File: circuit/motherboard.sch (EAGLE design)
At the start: 8 parts, among them IC1 ATMEGA8

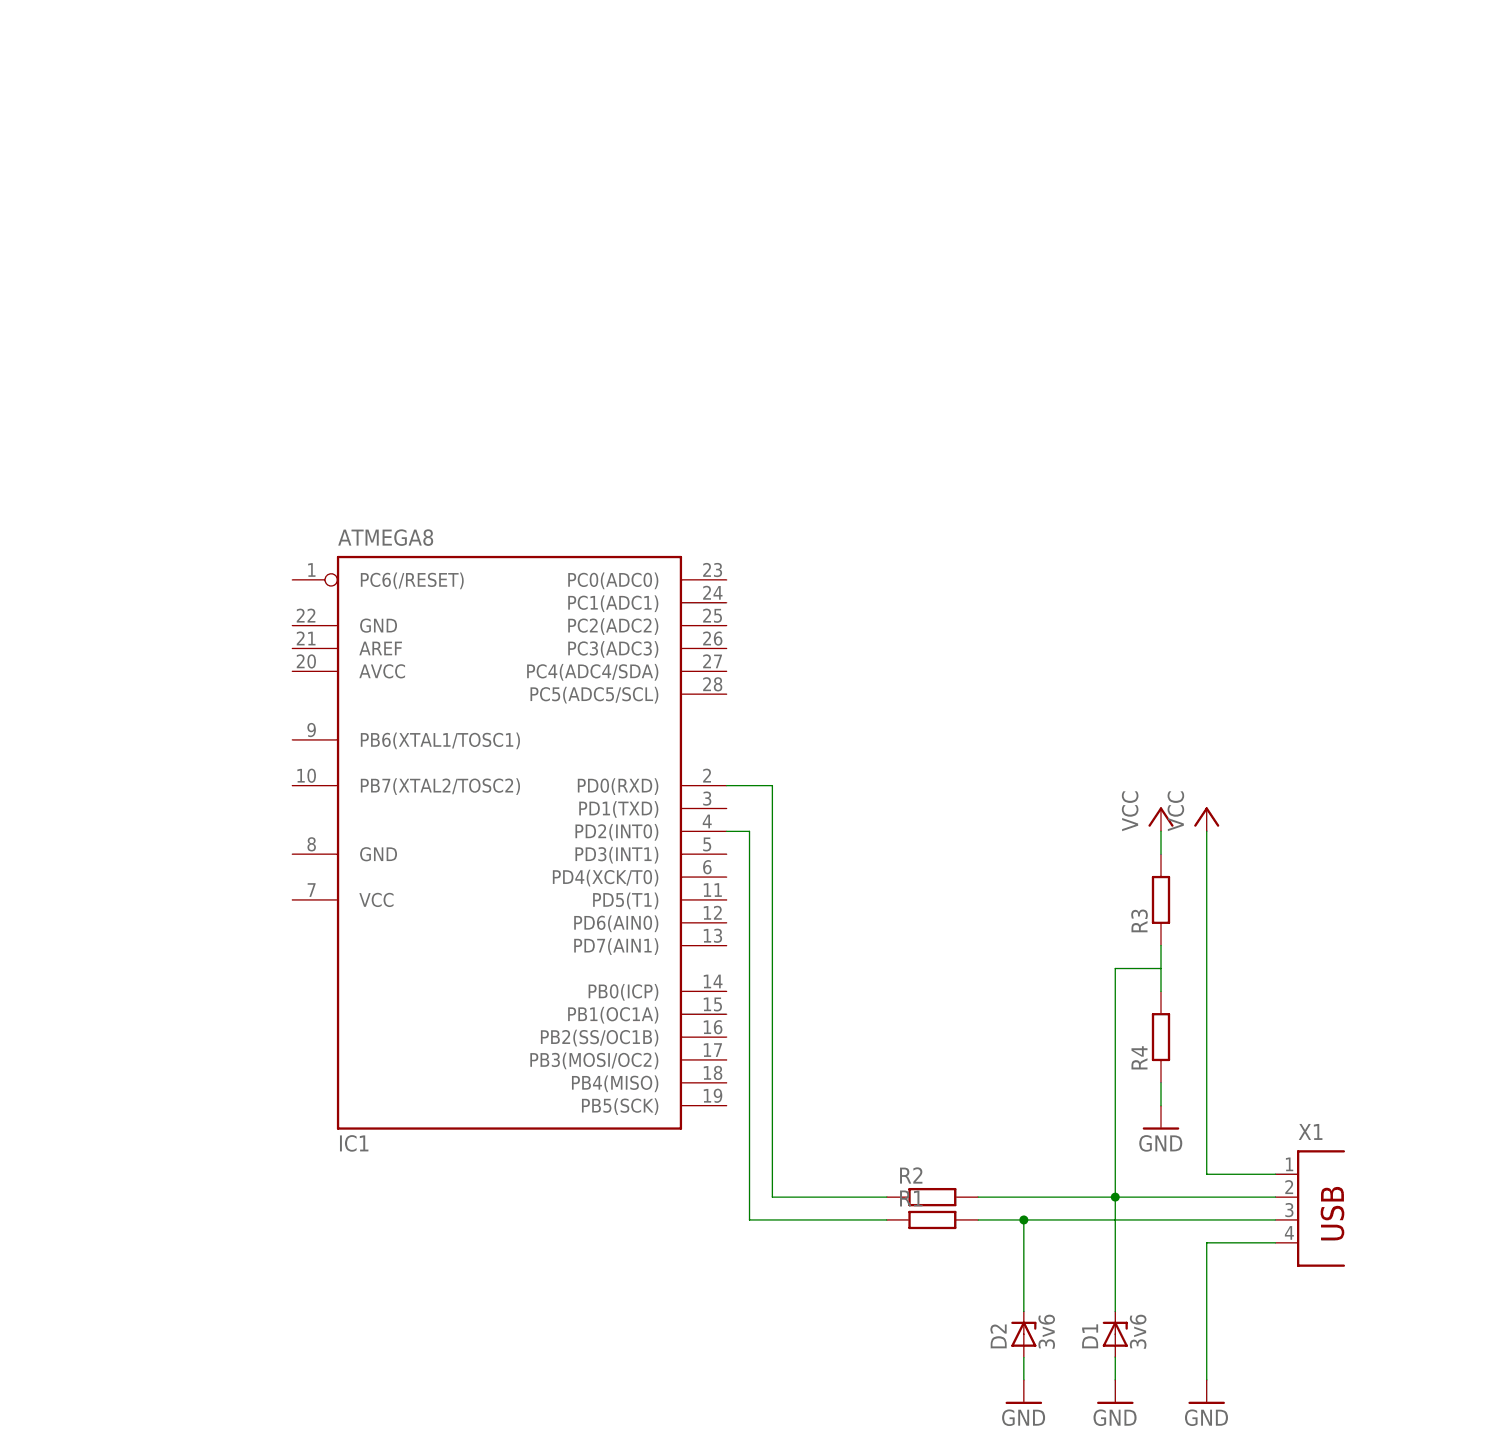
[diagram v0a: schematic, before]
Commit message: PCB layout done, add to tracking
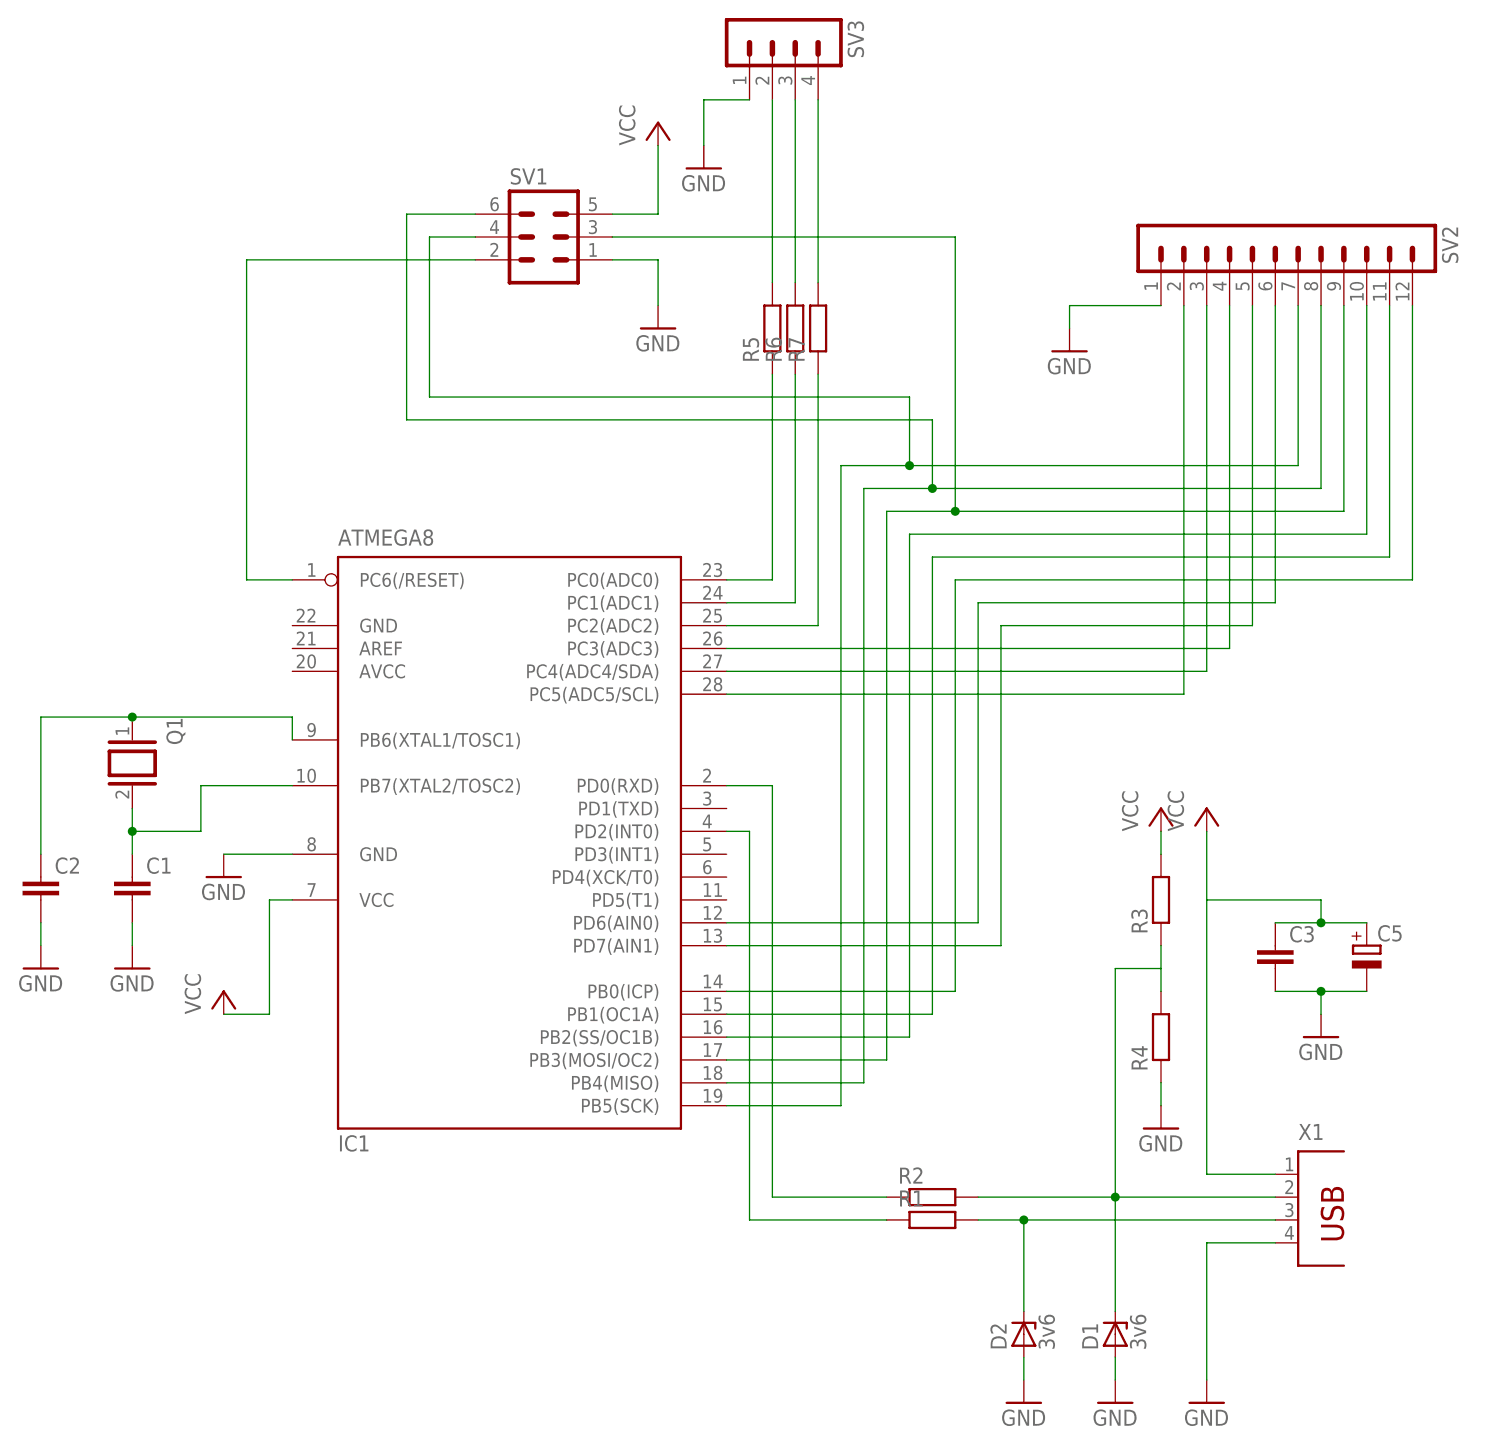
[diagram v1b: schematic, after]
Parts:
- added C1, C2, C3: (no value), rcl:C-EU050-024X044
- added C5: (no value), rcl:CPOL-EUB45181B
- added Q1: (no value), special:XTAL
- added R5, R6, R7: (no value), resistor:R-EU_0204/7
- added SV1: (no value), con-lstb:MA03-2
- added SV2: (no value), con-lstb:MA12-1
- added SV3: (no value), con-lstb:MA04-1
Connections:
- new net N$10: IC1.PB3(MOSI/OC2), SV1.3, SV2.9
- new net N$11: IC1.PB2(SS/OC1B), SV2.10
- new net N$12: IC1.PB1(OC1A), SV2.11
- new net N$13: IC1.PD6(AIN0), SV2.6
- new net N$14: IC1.PD7(AIN1), SV2.5
- new net N$15: IC1.PC3(ADC3), SV2.4
- new net N$16: IC1.PC4(ADC4/SDA), SV2.3
- new net N$17: IC1.PC5(ADC5/SCL), SV2.2
- new net N$18: IC1.PC6(/RESET), SV1.2
- new net N$19: R6.2, SV3.3
- new net N$20: IC1.PC2(ADC2), R7.1
- new net N$21: IC1.PC1(ADC1), R6.1
- new net N$22: IC1.PC0(ADC0), R5.1
- new net N$23: IC1.PB4(MISO), SV1.6, SV2.8
- new net N$24: R7.2, SV3.4
- new net N$5: C1.1, IC1.PB7(XTAL2/TOSC2), Q1.2
- new net N$6: C2.1, IC1.PB6(XTAL1/TOSC1), Q1.1
- new net N$7: IC1.PB5(SCK), SV1.4, SV2.7
- new net N$8: IC1.PB0(ICP), SV2.12
- new net N$9: R5.2, SV3.2
- net GND: now also C1.2, C2.2, C3.2, C5.-, IC1.GND@1, SV1.1, SV2.1, SV3.1
- net VCC: now also C3.1, C5.+, IC1.VCC@1, SV1.5

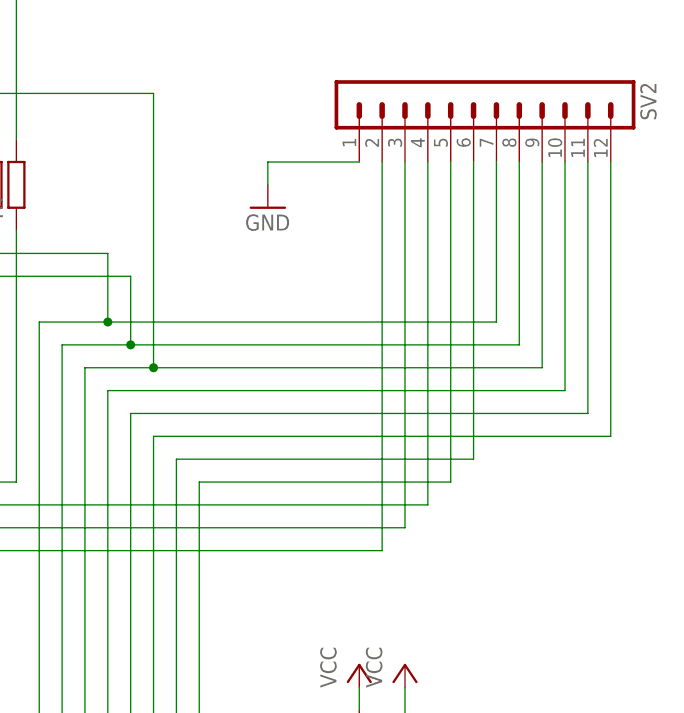
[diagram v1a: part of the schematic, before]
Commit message: New PCB design, minor chenges in schematic
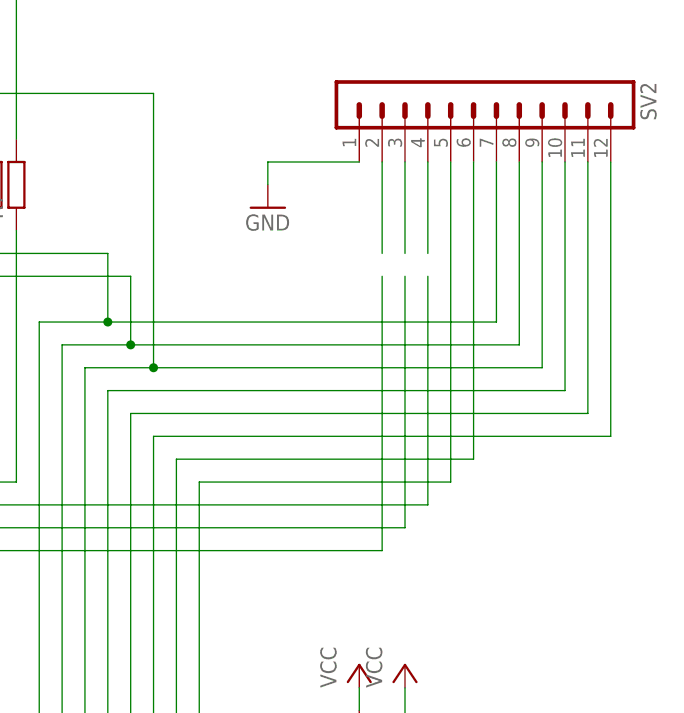
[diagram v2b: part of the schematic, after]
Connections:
- new net N$25: SV2.2
- new net N$26: SV2.3
- new net N$27: SV2.4
- net N$15: no longer SV2.4
- net N$16: no longer SV2.3
- net N$17: no longer SV2.2
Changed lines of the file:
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@@
 <grid distance="0.1" unitdist="inch" unit="inch" style="lines" multiple="1" display="no" altdistance="0.01" altunitdist="inch" altunit="inch"/>
 <layers>
-<layer number="1" name="Top" color="4" fill="1" visible="yes" active="no"/>
-<layer number="16" name="Bottom" color="1" fill="1" visible="yes" active="no"/>
-<layer number="17" name="Pads" color="2" fill="1" visible="yes" active="no"/>
-<layer number="18" name="Vias" color="2" fill="1" visible="yes" active="no"/>
-<layer number="19" name="Unrouted" color="6" fill="1" visible="yes" active="no"/>
-<layer number="20" name="Dimension" color="15" fill="1" visible="yes" active="no"/>
-<layer number="21" name="tPlace" color="7" fill="1" visible="yes" active="no"/>
-<layer number="22" name="bPlace" color="7" fill="1" visible="yes" active="no"/>
-<layer number="23" name="tOrigins" color="15" fill="1" visible="yes" active="no"/>
-<layer number="24" name="bOrigins" color="15" fill="1" visible="yes" active="no"/>
-<layer number="25" name="tNames" color="7" fill="1" visible="yes" active="no"/>
-<layer number="26" name="bNames" color="7" fill="1" visible="yes" active="no"/>
-<layer number="27" name="tValues" color="7" fill="1" visible="yes" active="no"/>
-<layer number="28" name="bValues" color="7" fill="1" visible="yes" active="no"/>
+<layer number="1" name="Top" color="4" fill="1" visible="no" active="no"/>
+<layer number="16" name="Bottom" color="1" fill="1" visible="no" active="no"/>
+<layer number="17" name="Pads" color="2" fill="1" visible="no" active="no"/>
+<layer number="18" name="Vias" color="2" fill="1" visible="no" active="no"/>
+<layer number="19" name="Unrouted" color="6" fill="1" visible="no" active="no"/>
+<layer number="20" name="Dimension" color="15" fill="1" visible="no" active="no"/>
+<layer number="21" name="tPlace" color="7" fill="1" visible="no" active="no"/>
+<layer number="22" name="bPlace" color="7" fill="1" visible="no" active="no"/>
+<layer number="23" name="tOrigins" color="15" fill="1" visible="no" active="no"/>
+<layer number="24" name="bOrigins" color="15" fill="1" visible="no" active="no"/>
+<layer number="25" name="tNames" color="7" fill="1" visible="no" active="no"/>
+<layer number="26" name="bNames" color="7" fill="1" visible="no" active="no"/>
+<layer number="27" name="tValues" color="7" fill="1" visible="no" active="no"/>
+<layer number="28" name="bValues" color="7" fill="1" visible="no" active="no"/>
 <layer number="29" name="tStop" color="7" fill="3" visible="no" active="no"/>
 <layer number="30" name="bStop" color="7" fill="6" visible="no" active="no"/>
@@
 <layer number="35" name="tGlue" color="7" fill="4" visible="no" active="no"/>
 <layer number="36" name="bGlue" color="7" fill="5" visible="no" active="no"/>
-<layer number="37" name="tTest" color="7" fill="1" visible="yes" active="no"/>
-<layer number="38" name="bTest" color="7" fill="1" visible="yes" active="no"/>
+<layer number="37" name="tTest" color="7" fill="1" visible="no" active="no"/>
+<layer number="38" name="bTest" color="7" fill="1" visible="no" active="no"/>
 <layer number="39" name="tKeepout" color="4" fill="11" visible="no" active="no"/>
 <layer number="40" name="bKeepout" color="1" fill="11" visible="no" active="no"/>
@@
 <layer number="44" name="Drills" color="7" fill="1" visible="no" active="no"/>
 <layer number="45" name="Holes" color="7" fill="1" visible="no" active="no"/>
-<layer number="46" name="Milling" color="3" fill="1" visible="yes" active="no"/>
-<layer number="47" name="Measures" color="7" fill="1" visible="yes" active="no"/>
-<layer number="48" name="Document" color="7" fill="1" visible="yes" active="no"/>
-<layer number="49" name="Reference" color="7" fill="1" visible="yes" active="no"/>
-<layer number="51" name="tDocu" color="7" fill="1" visible="yes" active="no"/>
-<layer number="52" name="bDocu" color="7" fill="1" visible="yes" active="no"/>
+<layer number="46" name="Milling" color="3" fill="1" visible="no" active="no"/>
+<layer number="47" name="Measures" color="7" fill="1" visible="no" active="no"/>
+<layer number="48" name="Document" color="7" fill="1" visible="no" active="no"/>
+<layer number="49" name="Reference" color="7" fill="1" visible="no" active="no"/>
+<layer number="51" name="tDocu" color="7" fill="1" visible="no" active="no"/>
+<layer number="52" name="bDocu" color="7" fill="1" visible="no" active="no"/>
 <layer number="91" name="Nets" color="2" fill="1" visible="yes" active="yes"/>
 <layer number="92" name="Busses" color="1" fill="1" visible="yes" active="yes"/>
@@
 </variantdefs>
 <classes>
-<class number="0" name="default" width="0" drill="0">
+<class number="0" name="default" width="0.4064" drill="0.508">
+<clearance class="0" value="0.254"/>
 </class>
 </classes>
@@
 <pinref part="IC1" gate="G$1" pin="PC3(ADC3)"/>
 <wire x1="66.04" y1="73.66" x2="121.92" y2="73.66" width="0.1524" layer="91"/>
-<wire x1="121.92" y1="73.66" x2="121.92" y2="111.76" width="0.1524" layer="91"/>
-<pinref part="SV2" gate="1" pin="4"/>
+<wire x1="121.92" y1="73.66" x2="121.92" y2="99.06" width="0.1524" layer="91"/>
 </segment>
 </net>
@@
 <pinref part="IC1" gate="G$1" pin="PC4(ADC4/SDA)"/>
 <wire x1="66.04" y1="71.12" x2="119.38" y2="71.12" width="0.1524" layer="91"/>
-<wire x1="119.38" y1="71.12" x2="119.38" y2="111.76" width="0.1524" layer="91"/>
-<pinref part="SV2" gate="1" pin="3"/>
+<wire x1="119.38" y1="71.12" x2="119.38" y2="99.06" width="0.1524" layer="91"/>
 </segment>
 </net>
@@
 <pinref part="IC1" gate="G$1" pin="PC5(ADC5/SCL)"/>
 <wire x1="66.04" y1="68.58" x2="116.84" y2="68.58" width="0.1524" layer="91"/>
-<wire x1="116.84" y1="68.58" x2="116.84" y2="111.76" width="0.1524" layer="91"/>
-<pinref part="SV2" gate="1" pin="2"/>
+<wire x1="116.84" y1="68.58" x2="116.84" y2="99.06" width="0.1524" layer="91"/>
 </segment>
 </net>
@@
 </segment>
 </net>
+<net name="N$25" class="0">
+<segment>
+<pinref part="SV2" gate="1" pin="2"/>
+<wire x1="116.84" y1="101.6" x2="116.84" y2="111.76" width="0.1524" layer="91"/>
+</segment>
+</net>
+<net name="N$26" class="0">
+<segment>
+<pinref part="SV2" gate="1" pin="3"/>
+<wire x1="119.38" y1="101.6" x2="119.38" y2="111.76" width="0.1524" layer="91"/>
+</segment>
+</net>
+<net name="N$27" class="0">
+<segment>
+<pinref part="SV2" gate="1" pin="4"/>
+<wire x1="121.92" y1="101.6" x2="121.92" y2="111.76" width="0.1524" layer="91"/>
+</segment>
+</net>
